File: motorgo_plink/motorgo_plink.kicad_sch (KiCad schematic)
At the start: 21 parts, among them J1 USB4520-03-0-A_REVA, J4 Conn_02x20_Odd_Even, U1 ESP32-S3-WROOM-1, U2 USBLC6-2P6

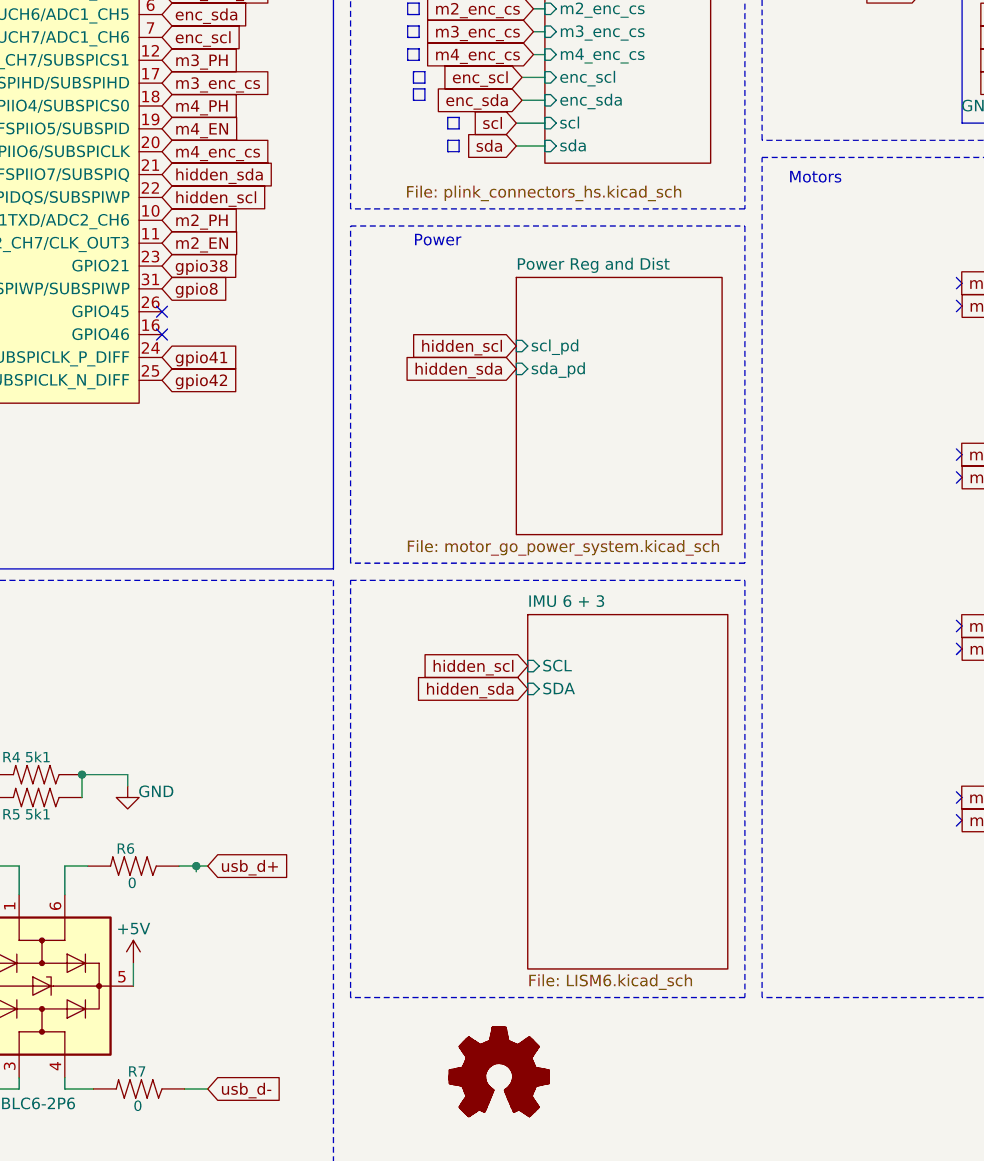
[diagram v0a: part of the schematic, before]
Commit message: wip culling of non-vital schematic components
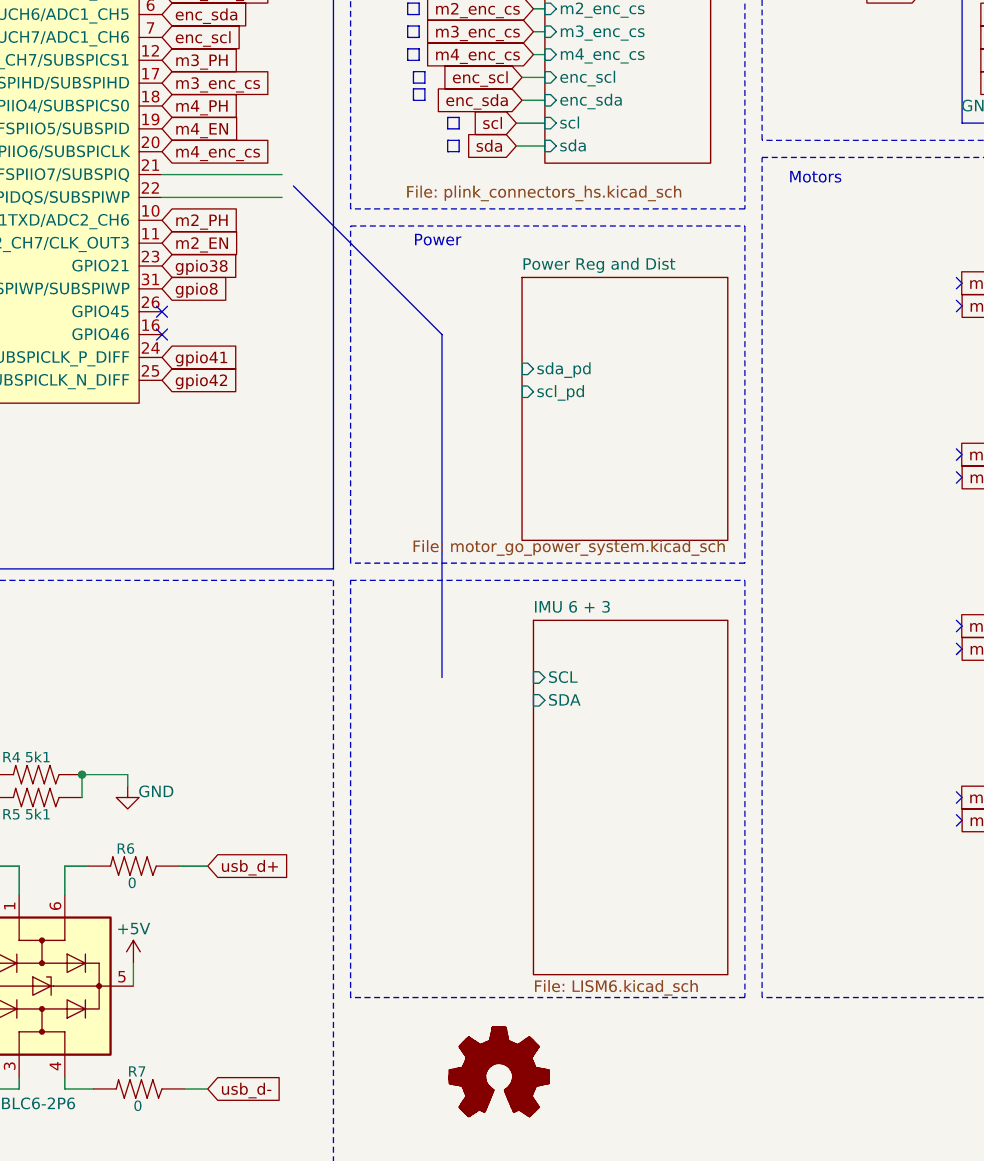
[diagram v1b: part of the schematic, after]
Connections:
- net hidden_scl: no longer names the net of U1.22 (GPIO14/TOUCH14/ADC2_CH3/FSPIWP/FSPIDQS/SUBSPIWP)
- net hidden_sda: no longer names the net of U1.21 (GPIO13/TOUCH13/ADC2_CH2/FSPIQ/FSPIIO7/SUBSPIQ)

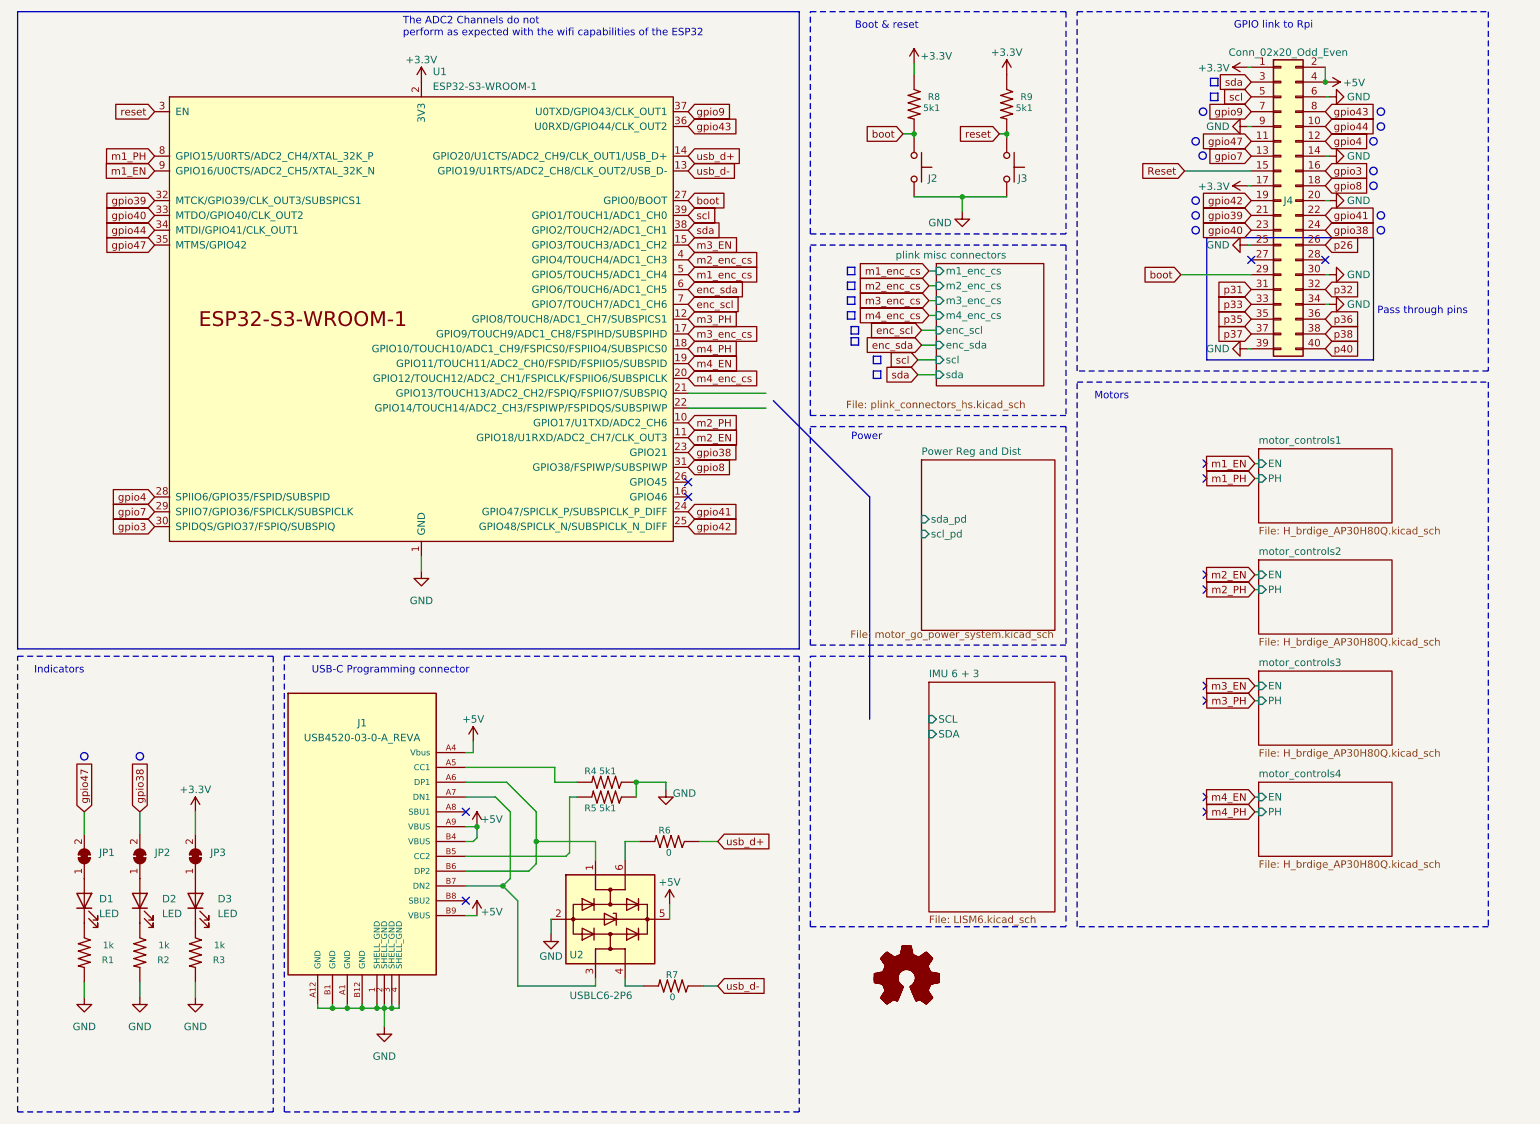
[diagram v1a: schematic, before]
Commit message: wip culling schematics and removing tracks
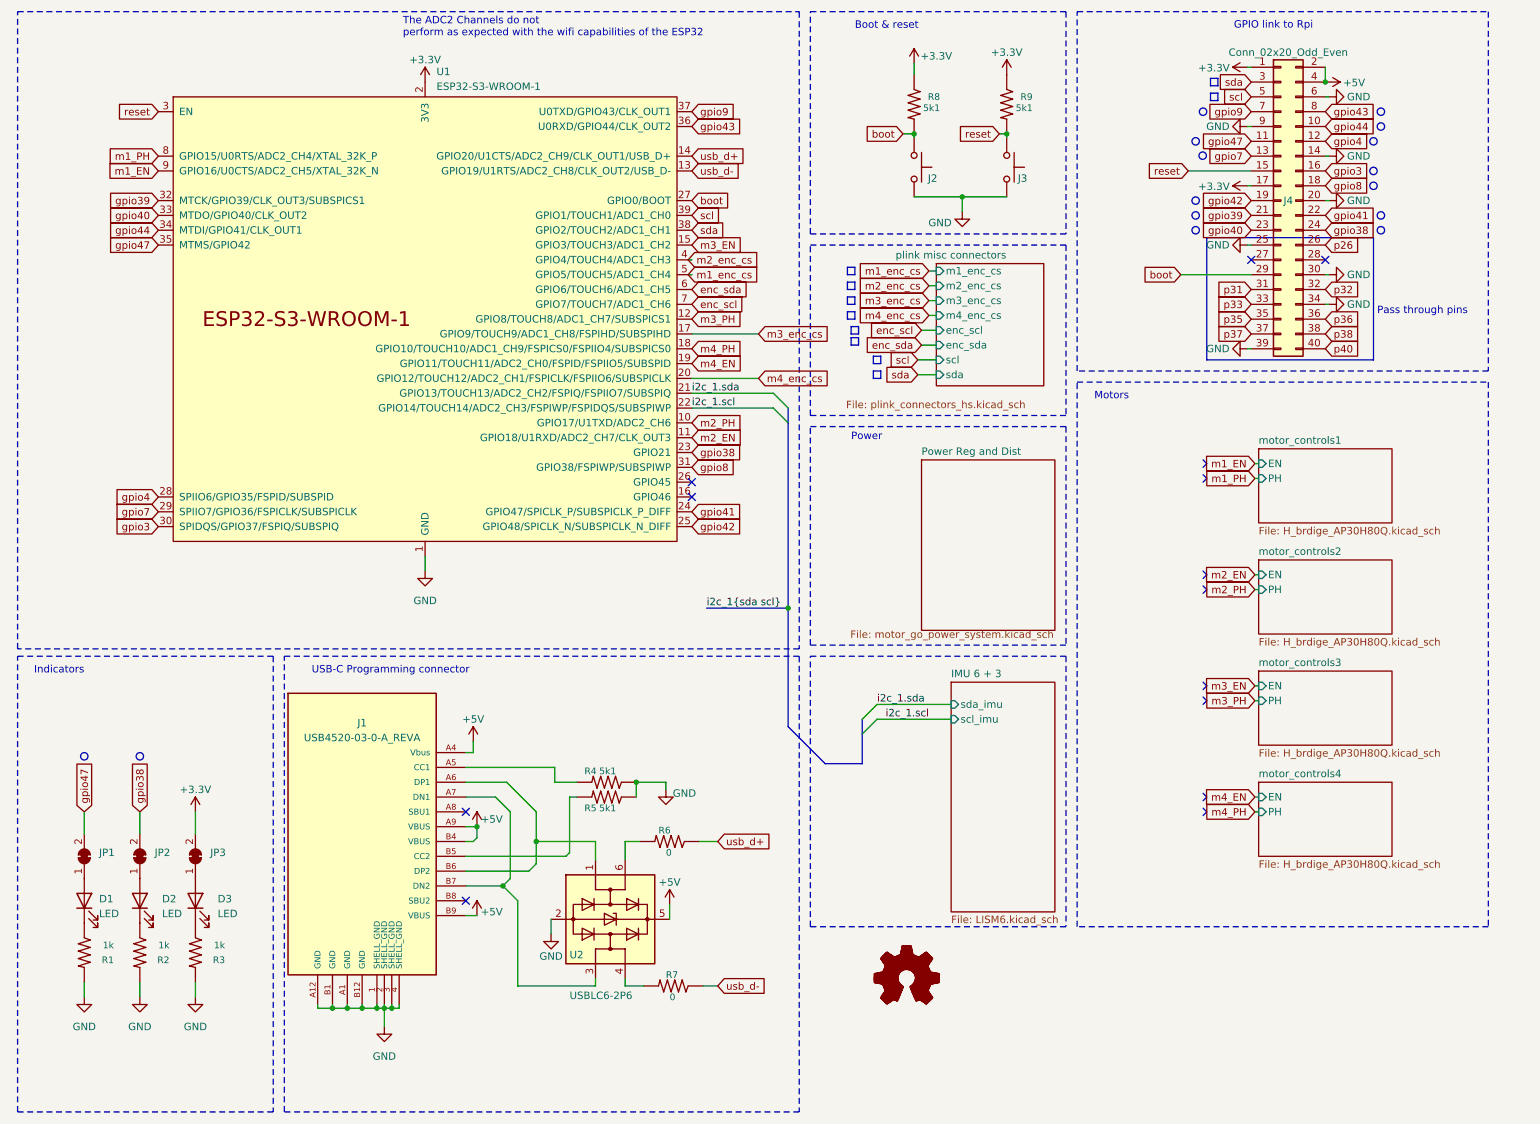
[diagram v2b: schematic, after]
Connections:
- net Reset is gone; now on net reset: J4.15 (Pin_15)
- net i2c_1.sda: now reaches U1.21 (GPIO13/TOUCH13/ADC2_CH2/FSPIQ/FSPIIO7/SUBSPIQ)
- net i2c_1.scl: now reaches U1.22 (GPIO14/TOUCH14/ADC2_CH3/FSPIWP/FSPIDQS/SUBSPIWP)
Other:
- sheet IMU 6 + 3 ports: added scl_imu, sda_imu; removed SCL, SDA
- sheet Power Reg and Dist ports: added none; removed scl_pd, sda_pd
- moved on the sheet: U1

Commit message: wip schematic edits to account for buck reg design
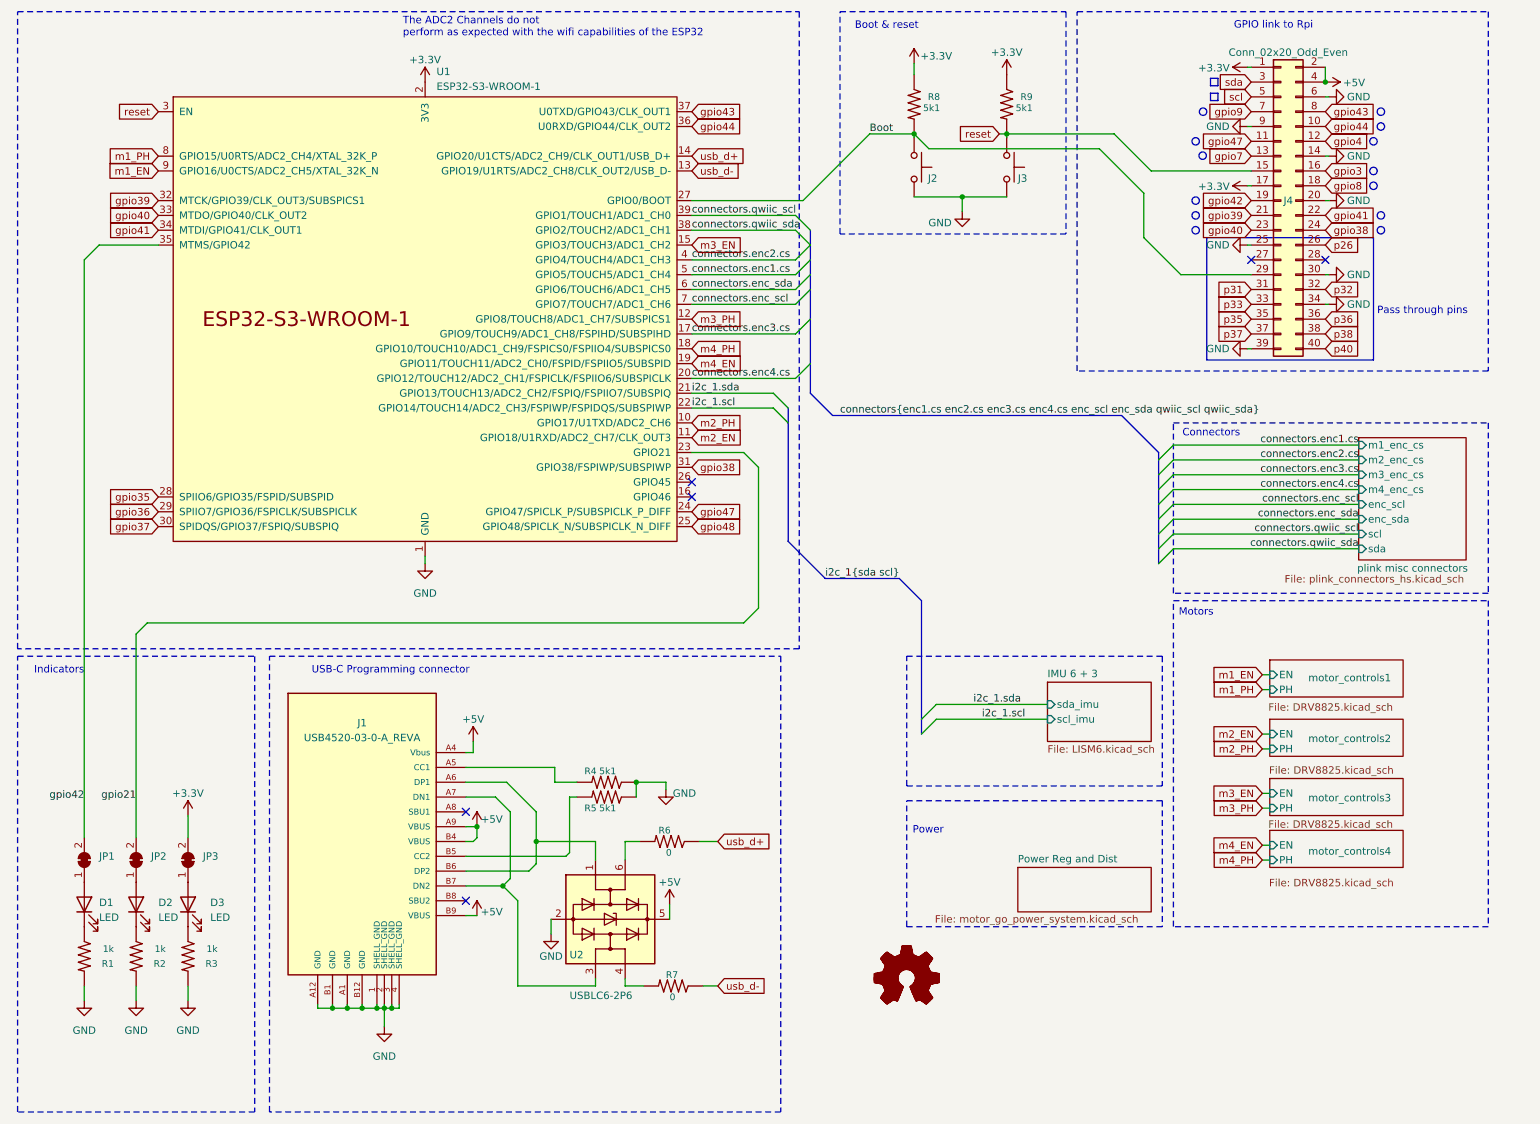
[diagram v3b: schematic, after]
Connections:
- net gpio3: no longer U1.30 (SPIDQS/GPIO37/FSPIQ/SUBSPIQ)
- net gpio38: now also U1.31 (GPIO38/FSPIWP/SUBSPIWP); no longer JP2.2 (B), U1.23 (GPIO21)
- net gpio4: no longer U1.28 (SPIIO6/GPIO35/FSPID/SUBSPID)
- net gpio41: now also U1.34 (MTDI/GPIO41/CLK_OUT1); no longer U1.24 (GPIO47/SPICLK_P/SUBSPICLK_P_DIFF)
- net gpio42: now also JP1.2 (B), U1.35 (MTMS/GPIO42); no longer U1.25 (GPIO48/SPICLK_N/SUBSPICLK_N_DIFF)
- net gpio43: now also U1.37 (U0TXD/GPIO43/CLK_OUT1); no longer U1.36 (U0RXD/GPIO44/CLK_OUT2)
- net gpio44: now also U1.36 (U0RXD/GPIO44/CLK_OUT2); no longer U1.34 (MTDI/GPIO41/CLK_OUT1)
- net gpio47: now also U1.24 (GPIO47/SPICLK_P/SUBSPICLK_P_DIFF); no longer JP1.2 (B), U1.35 (MTMS/GPIO42)
- net gpio7: no longer U1.29 (SPIIO7/GPIO36/FSPICLK/SUBSPICLK)
- net gpio8: no longer U1.31 (GPIO38/FSPIWP/SUBSPIWP)
- net gpio9: no longer U1.37 (U0TXD/GPIO43/CLK_OUT1)
- net scl: no longer U1.39 (GPIO1/TOUCH1/ADC1_CH0)
- net sda: no longer U1.38 (GPIO2/TOUCH2/ADC1_CH1)
- net boot renamed Boot
- net enc_scl renamed connectors.enc_scl
- net enc_sda renamed connectors.enc_sda
- net m1_enc_cs renamed connectors.enc1.cs
- net m2_enc_cs renamed connectors.enc2.cs
- net m3_enc_cs renamed connectors.enc3.cs
- net m4_enc_cs renamed connectors.enc4.cs
- new net connectors.qwiic_scl: U1.39 (GPIO1/TOUCH1/ADC1_CH0)
- new net connectors.qwiic_sda: U1.38 (GPIO2/TOUCH2/ADC1_CH1)
- new net gpio21: JP2.2 (B), U1.23 (GPIO21)
- new net gpio35: U1.28 (SPIIO6/GPIO35/FSPID/SUBSPID)
- new net gpio36: U1.29 (SPIIO7/GPIO36/FSPICLK/SUBSPICLK)
- new net gpio37: U1.30 (SPIDQS/GPIO37/FSPIQ/SUBSPIQ)
- new net gpio48: U1.25 (GPIO48/SPICLK_N/SUBSPICLK_N_DIFF)
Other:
- sheet motor_controls1: file H_brdige_AP30H80Q.kicad_sch -> DRV8825.kicad_sch
- sheet motor_controls2: file H_brdige_AP30H80Q.kicad_sch -> DRV8825.kicad_sch
- sheet motor_controls3: file H_brdige_AP30H80Q.kicad_sch -> DRV8825.kicad_sch
- sheet motor_controls4: file H_brdige_AP30H80Q.kicad_sch -> DRV8825.kicad_sch
- note added: "Connectors"
- moved on the sheet: D1, D2, D3, JP1, JP2, JP3, R1, R2, R3
